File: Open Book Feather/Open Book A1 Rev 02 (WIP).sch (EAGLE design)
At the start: 127 parts, among them J1 SJ-43514-SMT, J2 10118193-0001LF, Q1 DMG341, Q2 IRLML0100, SW1 SPDT_SWITCH, U1 AP2112-3.3, U2 MCP73831T-2ACI/OT, U3 ATSAMD51J64-TQFP(10X10), U4 GD25Q16C (or GD25Q32C), U5 74AC165D, U6 GD25Q16C (or GD25Q32C), U7 23K256-I/SN, U8 MAX4466EXK+T, X1 JSTPH, X2 2x5 0.05" SWD

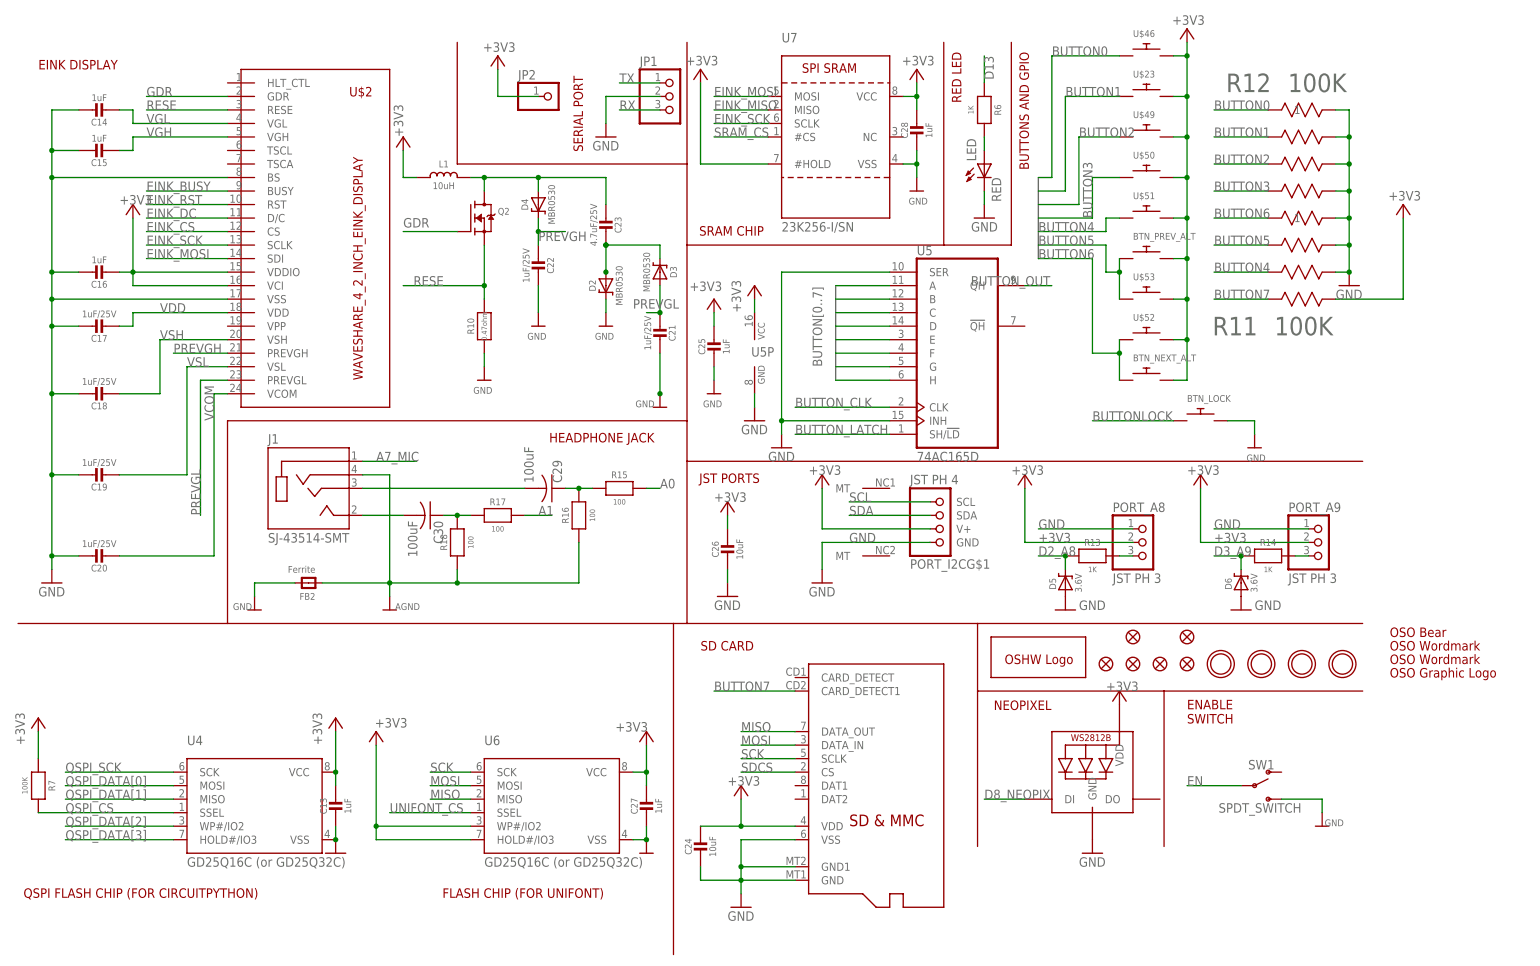
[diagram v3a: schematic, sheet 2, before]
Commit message: renumber passives
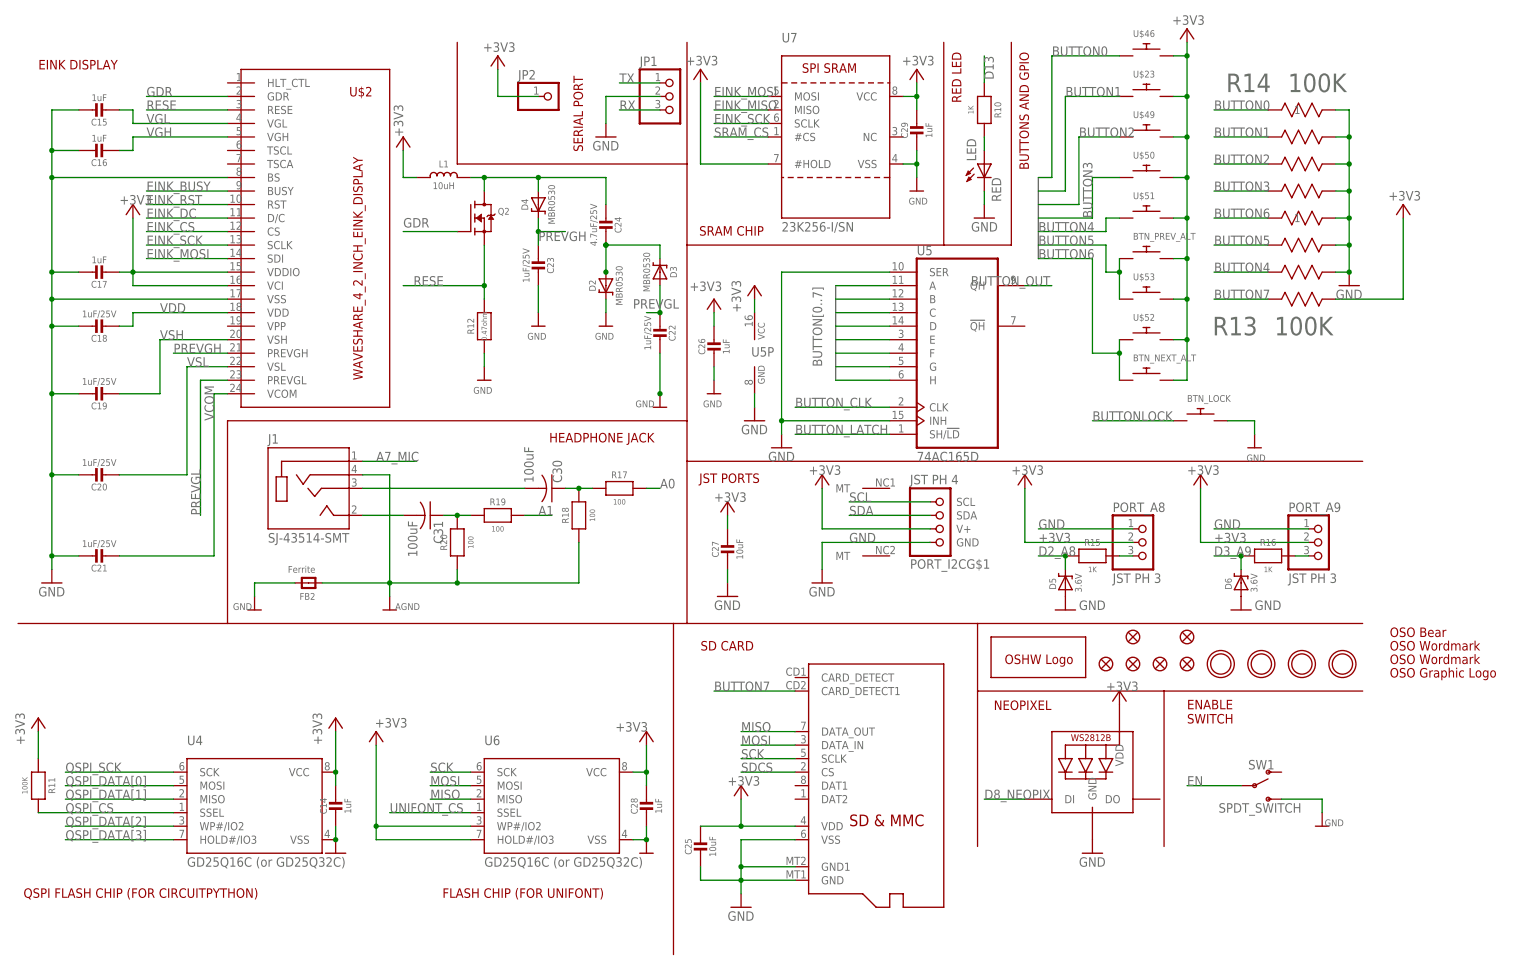
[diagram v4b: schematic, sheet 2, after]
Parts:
- C13: value 1uF -> 0.1uF; device microbuilder:CAP_CERAMIC0805-NOOUTLINE -> microbuilder:CAP_CERAMIC0805_10MGAP
- C17: value 1uF/25V -> 1uF
- C23: value 4.7uF/25V -> 1uF/25V
- C24: value 10uF -> 4.7uF/25V; device microbuilder:CAP_CERAMIC0805_10MGAP -> microbuilder:CAP_CERAMIC0805-NOOUTLINE
- C25: value 1uF -> 10uF
- C26: value 10uF -> 1uF; device microbuilder:CAP_CERAMIC0805-NOOUTLINE -> microbuilder:CAP_CERAMIC0805_10MGAP
- C27: value 1uF -> 10uF; device microbuilder:CAP_CERAMIC0805_10MGAP -> microbuilder:CAP_CERAMIC0805-NOOUTLINE
- C29: value 100uF -> 1uF; device resistor:C-USC1210 -> microbuilder:CAP_CERAMIC0805_10MGAP
- C31: value 0.1µF -> 100uF; device microbuilder:CAP_CERAMIC0805-NOOUTLINE -> resistor:C-USC1210
- C32: value 0.01uF -> 0.1µF
- C33: value 100pF -> 0.01uF
- C34: value 10uF -> 100pF
- C35: value 0.1uF -> 10uF; device microbuilder:CAP_CERAMIC0805_10MGAP -> microbuilder:CAP_CERAMIC0805-NOOUTLINE
- R10: value 0.47ohm -> 1K; device microbuilder:RESISTOR0805_10MGAP -> microbuilder:RESISTOR0805_NOOUTLINE
- R11: device resistor array:EXB-V8V103JV -> microbuilder:RESISTOR0805_NOOUTLINE
- R12: value 100K -> 0.47ohm; device resistor array:EXB-V8V103JV -> microbuilder:RESISTOR0805_10MGAP
- R13, R14: value 1K -> 100K; device microbuilder:RESISTOR_0805MP -> resistor array:EXB-V8V103JV
- R15, R16: value 100 -> 1K; device microbuilder:RESISTOR0805_NOOUTLINE -> microbuilder:RESISTOR_0805MP
- R19, R20: value 1K -> 100
- R21, R22: value 1M -> 1K
- R23: value 1K -> 1M
- R24: value 100K -> 1M
- R25: value 10K -> 1K; device microbuilder:RESISTOR0805_10MGAP -> microbuilder:RESISTOR0805_NOOUTLINE
- R26: value 100 -> 100K; device microbuilder:RESISTOR0805_10MGAP -> microbuilder:RESISTOR0805_NOOUTLINE
- R3: value 10K\ -> 10K
- R6: value 1K -> 10K; device microbuilder:RESISTOR0805_NOOUTLINE -> microbuilder:RESISTOR0805_10MGAP
- R7: value 100K -> 100; device microbuilder:RESISTOR0805_NOOUTLINE -> microbuilder:RESISTOR0805_10MGAP
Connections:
- removed net N$70 (its old number): C29.1, R15.1, R16.2
- new net N$15: C31.1, R19.1, R20.2
- net !RESET: now also C13.2, R6.2, R7.2; no longer C35.2, R25.2, R26.2
- net +3V3: now also C14.1, C17.2, C29.1, R11.1, R13.5, R6.1; no longer C13.1, C16.2, C24.1, R11.5, R25.1, R7.1
- net A0: now also R17.2; no longer R15.2
- net A1: now also R19.2; no longer R17.2
- net A10_MICAMP: now also C34.1, R26.2; no longer C33.1, R24.2
- net A7_MIC: now also C33.1, R21.1; no longer C32.1, R19.1
- net A8_: now also R15.1; no longer R13.1
- net A9_: now also R16.1; no longer R14.1
- net AGND: now also C32.2, C35.2, R20.1, R23.1; no longer C31.2, C34.2, R16.1, R21.1
- net AUDIO_LEFT: now also C31.2; no longer C30.2
- net AUDIO_RIGHT: now also C30.2; no longer C29.2
- net AVCC: now also R24.2; no longer R20.2
- net BUTTON0: now also R14.1; no longer R12.1
- net BUTTON1: now also R14.2; no longer R12.2
- net BUTTON2: now also R14.3; no longer R12.3
- net BUTTON3: now also R14.4; no longer R12.4
- net BUTTON4: now also R13.3; no longer R11.3
- net BUTTON5: now also R13.2; no longer R11.2
- net BUTTON6: now also R13.1; no longer R11.1
- net BUTTON7: now also R13.4; no longer R11.4
- net D13: now also R10.1; no longer R6.1
- net D2_A8: now also R15.2; no longer R13.2
- net D3_A9: now also R16.2; no longer R14.2
- net GND: now also C13.1, C14.2, C21.1, C23.2, C29.2, R12.2, R13.6, R13.7, R13.8, R14.5, R14.6, R14.7, R14.8; no longer C13.2, C14.1, C21.2, C24.2, C35.1, R10.2, R11.6, R11.7, R11.8, R12.5, R12.6, R12.7, R12.8
- net N$1: now also R7.1; no longer R26.1
- net N$2: now also C24.2; no longer C23.2
- net N$3: now also C24.1; no longer C23.1
- net N$65: now also C32.1, R21.2, R22.1; no longer C31.1, R19.2, R20.1
- net N$67: now also C33.2, R23.2, R24.1; no longer C32.2, R21.2, R22.1
- net N$68: now also C34.2, R25.1, R26.1; no longer C33.2, R23.1, R24.1
- net N$69: now also C35.1, R25.2; no longer C34.1, R23.2
- net N$7: now also R10.2; no longer R6.2
- net PREVGH: now also C23.1; no longer C22.1
- net PREVGL: now also C22.1; no longer C21.1
- net QSPI_CS: now also R11.2; no longer R7.2
- net RESE: now also R12.1; no longer R10.1
- net VCOM: now also C21.2; no longer C20.2
- net VDD: now also C18.2; no longer C17.2
- net VGH: now also C16.2; no longer C15.2
- net VGL: now also C15.2; no longer C14.2
- net VSH: now also C19.2; no longer C18.2
- net VSL: now also C20.2; no longer C19.2
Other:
- note added: "Low pass F3db = 1/R25*C35*2pi"
- note added: "R25"
- note added: "R26"
- note removed: "Low pass F3db = 1/R23*C34*2pi"
- note removed: "R23"
- note removed: "R24"
- moved on the sheet: C14, C15, C16, C17, C18, C19, C20, C21, C22, C23, C24, C25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
